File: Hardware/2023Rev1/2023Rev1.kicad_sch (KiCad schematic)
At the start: 100 parts, among them J1 Conn_01x09, J2 Conn_01x09, J3 Conn_01x04, J4 Conn_01x03, Q1 Q_NMOS_GDS, Q2 Q_NMOS_DGS, SW1 SW_SPDT, SW1 SW_SPST, U1 Teensy4.1_DEV-16771, U10 LT1910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

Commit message: Labeling changes
Added labels to voltage sense conns
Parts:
- SW1: value SW_SPDT -> (none); footprint MRDT_Connectors:MOLEX_SL_03_Horizontal -> (none)
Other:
- company: MRDT - Drew Wellen, Cole Renken, Jesse ? -> MRDT - Drew Wellen, Cole Renken, Jesse Deuel
- moved on the sheet: J1

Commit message: changed page size
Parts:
- SW1: value (none) -> SW_SPDT; footprint (none) -> MRDT_Connectors:MOLEX_SL_03_Horizontal
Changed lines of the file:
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@@
 (kicad_sch (version 20211123) (generator eeschema)
-  (paper "A3")
+  (paper "USLegal")
   (title_block
     (title "2023 BMS")
@@
       (effects (font (size 1.27 1.27)) (justify right))
     )
-    (property "Value" "" (id 1) (at 269.24 75.1839 90)
+    (property "Value" "SW_SPDT" (id 1) (at 269.24 75.1839 90)
       (effects (font (size 1.27 1.27)) (justify right))
     )
-    (property "Footprint" "" (id 2) (at 265.43 73.914 0)
-      (effects (font (size 1.27 1.27)) hide)
-    )
+    (property "Footprint" "MRDT_Connectors:MOLEX_SL_03_Horizontal" (id 2) (at 265.43 73.914 0)
+      (effects (font (size 1.27 1.27)) hide)
+    )

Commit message: Rearranged Components to fit new page size
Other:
- note added: "Teensy + Friends"
- note removed: "Teensy and Friends"
- moved on the sheet: BZ1, C2, C3, C4, C5, C6, C7, C8, Conn1A, Conn1B, D1, D10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

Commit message: Ran ERC and fixed some misc problems
-Labels
-Op Amp Annotations
-Rearranged aux power section
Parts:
- renumbered U2 to U3, U3 to U5, U5 to U7, U7 to U8
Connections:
- net cell1-sense is gone; now on net Cell1-SENSE: U1.14 (A0)
- net cell2-sense is gone; now on net Cell2-SENSE: U1.15 (A1)
- net cell3-sense is gone; now on net Cell3-SENSE: U1.16 (A2)
- net cell4-sense is gone; now on net Cell4-SENSE: U1.17 (A3)
- net cell5-sense is gone; now on net Cell5-SENSE: U1.18 (A4)
- net cell6-sense is gone; now on net Cell6-SENSE: U1.19 (A5)
- net cell7-sense is gone; now on net Cell7-SENSE: U1.20 (A6)
- net cell8-sense is gone; now on net Cell8-SENSE: U1.21 (A7)
- net +3.3V: now also C3.1
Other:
- moved on the sheet: C3, F1, SW1, U8C

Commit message: Adding PDF
PDF for PDR
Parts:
- D12: value PACK -> PACK_OUT
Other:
- note added: "Teensy & Friends"
- note removed: "Teensy + Friends"
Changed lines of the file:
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@@
   (junction (at 262.89 17.145) (diameter 0) (color 0 0 0 0)
   )
+  (junction (at 245.11 40.005) (diameter 0) (color 0 0 0 0)
+  )
   (junction (at 184.785 165.735) (diameter 0) (color 0 0 0 0)
   )
@@
   (junction (at 294.64 20.955) (diameter 0) (color 0 0 0 0)
   )
-  (junction (at 245.11 40.005) (diameter 0) (color 0 0 0 0)
-  )
   (junction (at 156.845 180.975) (diameter 0) (color 0 0 0 0)
   )
@@
     (stroke (width 0) (type default) (color 0 0 0 0))
   )
-  (wire (pts (xy 245.11 40.005) (xy 245.11 50.8))
-    (stroke (width 0) (type default) (color 0 0 0 0))
-  )
   (wire (pts (xy 218.44 153.67) (xy 218.44 163.83))
     (stroke (width 0) (type default) (color 0 0 0 0))
@@
     (stroke (width 0) (type default) (color 0 0 0 0))
   )
+  (wire (pts (xy 245.11 40.005) (xy 245.11 48.895))
+    (stroke (width 0) (type default) (color 0 0 0 0))
+  )
   (wire (pts (xy 118.745 165.735) (xy 118.745 169.545))
     (stroke (width 0) (type default) (color 0 0 0 0))
@@
     (stroke (width 0) (type default) (color 0 0 0 0))
   )
-  (wire (pts (xy 244.475 48.895) (xy 245.11 50.8))
-    (stroke (width 0) (type default) (color 0 0 0 0))
-  )
   (wire (pts (xy 170.815 147.955) (xy 173.355 147.955))
     (stroke (width 0) (type default) (color 0 0 0 0))
@@
     (stroke (width 0) (type default) (color 0 0 0 0))
   )
+  (wire (pts (xy 244.475 48.895) (xy 245.11 48.895))
+    (stroke (width 0) (type default) (color 0 0 0 0))
+  )
   (polyline (pts (xy 338.455 15.875) (xy 338.455 13.335))
     (stroke (width 0) (type default) (color 0 0 0 0))
@@
     (effects (font (size 2.5 2.5)) (justify left bottom))
   )
-  (text "Teensy + Friends" (at 132.08 118.11 0)
+  (text "Teensy & Friends" (at 132.08 118.11 0)
     (effects (font (size 2.5 2.5)) (justify left bottom))
   )
@@
     (in_bom yes) (on_board yes)
     (property "Reference" "D12" (id 0) (at 145.415 33.02 0))
-    (property "Value" "PACK" (id 1) (at 145.415 27.94 0))
+    (property "Value" "PACK_OUT" (id 1) (at 145.415 27.305 0))
     (property "Footprint" "LED_SMD:LED_0603_1608Metric_Pad1.05x0.95mm_HandSolder" (id 2) (at 145.415 30.48 0)
       (effects (font (size 1.27 1.27)) hide)
@@
     )
     (path "/0c078835-a97a-4231-9c97-76d6e4fb1941"
-      (reference "D12") (unit 1) (value "PACK") (footprint "LED_SMD:LED_0603_1608Metric_Pad1.05x0.95mm_HandSolder")
+      (reference "D12") (unit 1) (value "PACK_OUT") (footprint "LED_SMD:LED_0603_1608Metric_Pad1.05x0.95mm_HandSolder")
     )
     (path "/81187ef8-a89f-4382-a9cd-107587c14c9d"

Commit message: aligned to grid
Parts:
- removed SW1: SW_SPST, MRDT_Connectors:MOLEX_SL_03_Horizontal, symbol Switch:SW_SPST
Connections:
- net +5V: no longer C2.1, C5.1, SW1.2 (B), U6.1 (Vi), U9.1 (Vin)
- net PACK_OUT: no longer Q1.3 (S), V3.1
- net at C8.1, Q1.2 (D), U10.6 (SENSE)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: no longer F1.1, U4.5 (IP-)
- new net: C2.1, C5.1, SW1.2 (B), U6.1 (Vi), U9.1 (Vin)
- new net: Q1.3 (S), V3.1
- new net: F1.1, U4.5 (IP-)
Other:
- note added: "E-Switch"
- note removed: "SPST Switch"
- moved on the sheet: BZ1, C2, C3, C4, C5, C6, C7, C8, Conn1A, Conn1B, D1, D10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

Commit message: more grid fixes
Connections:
- net PACK_OUT: now also Q1.3 (S), V3.1
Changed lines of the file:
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@@
   (junction (at 163.83 149.86) (diameter 0) (color 0 0 0 0)
+  )
+  (junction (at 243.84 40.64) (diameter 0) (color 0 0 0 0)
   )
   (junction (at 76.2 165.1) (diameter 0) (color 0 0 0 0)
@@
     (stroke (width 0) (type default) (color 0 0 0 0))
   )
+  (wire (pts (xy 243.84 40.64) (xy 243.84 49.53))
+    (stroke (width 0) (type default) (color 0 0 0 0))
+  )
   (wire (pts (xy 17.78 180.34) (xy 24.13 180.34))
     (stroke (width 0) (type default) (color 0 0 0 0))
@@
     (stroke (width 0) (type default) (color 0 0 0 0))
   )
-  (wire (pts (xy 242.57 40.64) (xy 245.11 40.64))
+  (wire (pts (xy 242.57 40.64) (xy 243.84 40.64))
     (stroke (width 0) (type default) (color 0 0 0 0))
   )
@@
     (stroke (width 0) (type default) (color 0 0 0 0))
   )
+  (wire (pts (xy 242.57 49.53) (xy 243.84 49.53))
+    (stroke (width 0) (type default) (color 0 0 0 0))
+  )
   (wire (pts (xy 325.12 62.23) (xy 334.01 62.23))
     (stroke (width 0) (type default) (color 0 0 0 0))
@@
   )
   (wire (pts (xy 210.82 26.67) (xy 210.82 27.94))
+    (stroke (width 0) (type default) (color 0 0 0 0))
+  )
+  (wire (pts (xy 243.84 40.64) (xy 245.11 40.64))
     (stroke (width 0) (type default) (color 0 0 0 0))
   )
@@
     )
   )
-  (global_label "PACK_OUT" (shape output) (at 243.84 49.53 180) (fields_autoplaced)
-    (effects (font (size 1.27 1.27)) (justify right))
-    (property "Intersheet References" "${INTERSHEET_REFS}" (id 0) (at 231.9321 49.6094 0)
-      (effects (font (size 1.27 1.27)) (justify right) hide)
-    )
+  (global_label "PACK_OUT" (shape output) (at 242.57 49.53 180) (fields_autoplaced)
+    (effects (font (size 1.27 1.27)) (justify right))
+    (property "Intersheet References" "${INTERSHEET_REFS}" (id 0) (at 230.6621 49.6094 0)
+      (effects (font (size 1.27 1.27)) (justify right) hide)
+    )

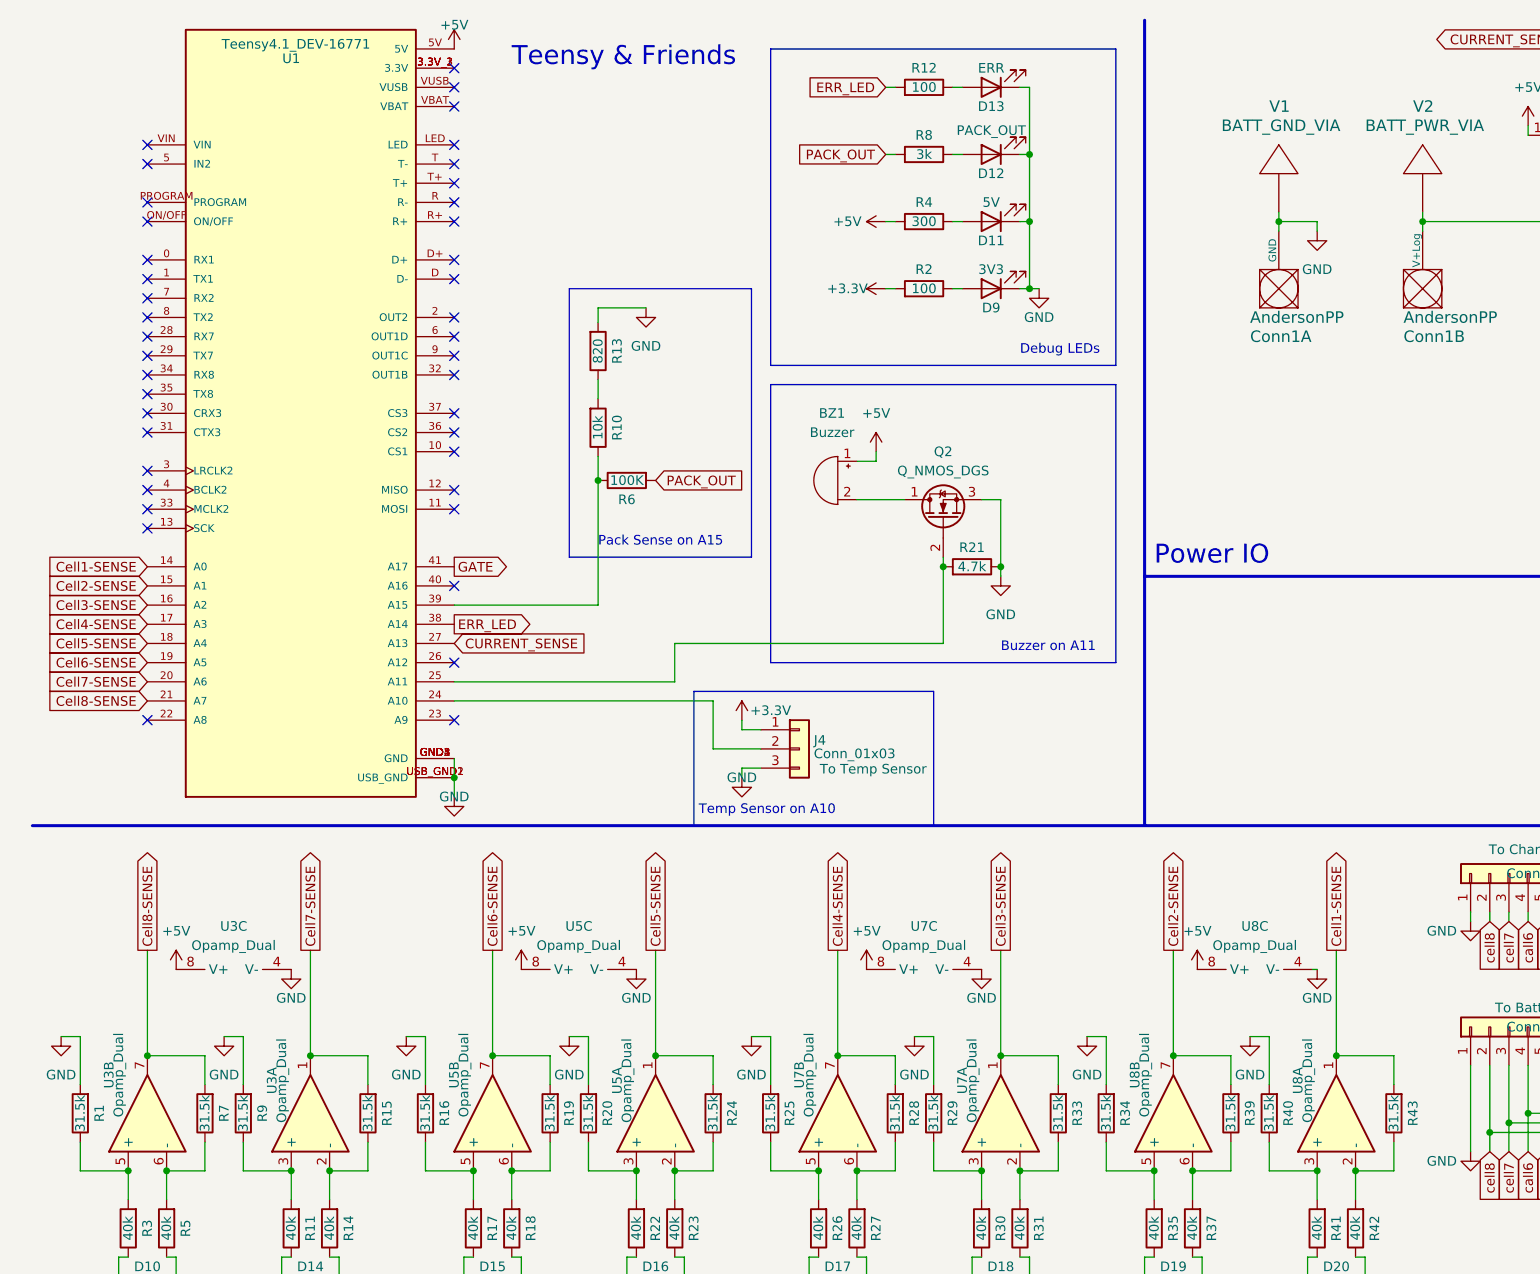
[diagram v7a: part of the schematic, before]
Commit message: Updated to BOM
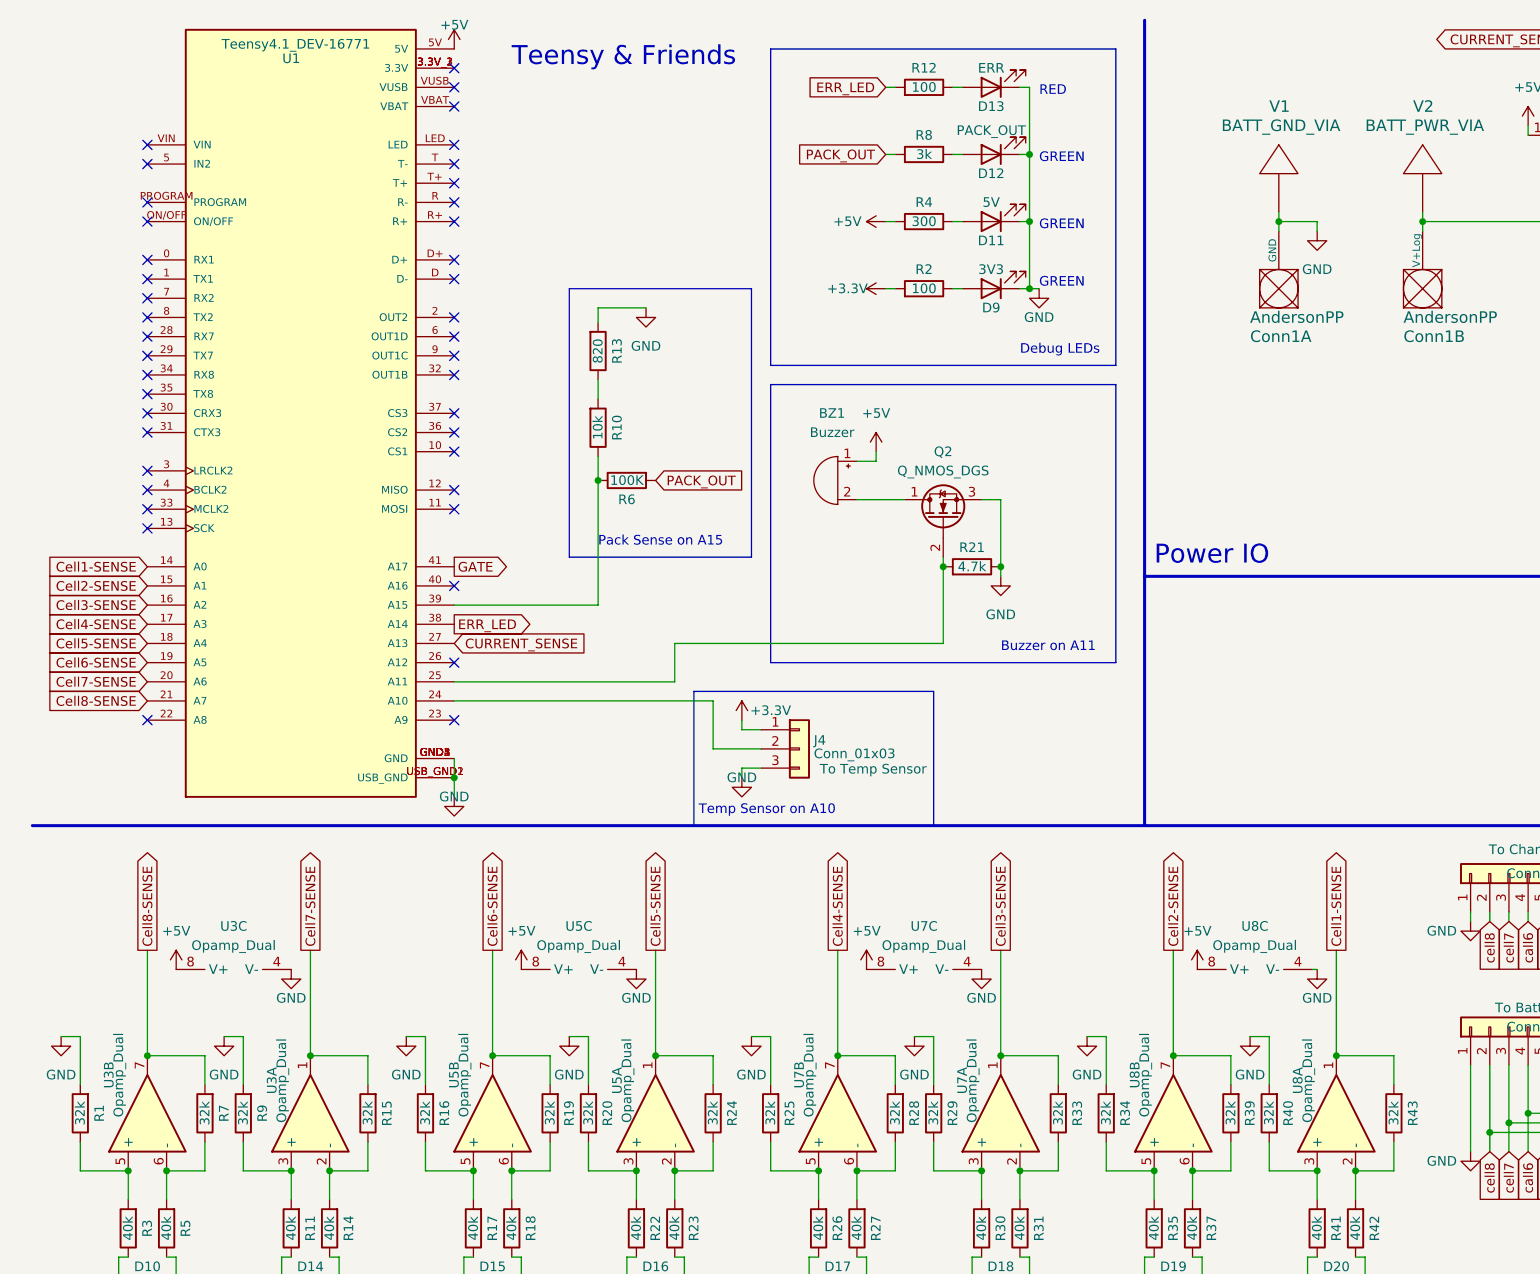
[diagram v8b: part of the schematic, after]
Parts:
- D1, D2, D3, D4, D5, D6, D7, D8: footprint Diode_SMD:D_0603_1608Metric_Pad1.05x0.95mm_HandSolder -> Package_TO_SOT_SMD:SOT-23
- D10, D14, D15, D16, D17, D18, D19, D20: footprint Diode_SMD:D_0603_1608Metric_Pad1.05x0.95mm_HandSolder -> Diode_SMD:D_SOD-523
- R1, R15, R16, R19, R20, R24, R25, R28, R29, R33, R34, R39, R40, R43, R7, R9: value 31.5k -> 32k
- U3, U5, U7, U8: footprint (none) -> Package_SO:SO-8_3.9x4.9mm_P1.27mm
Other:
- note added: "GREEN"
- note added: "RED"
